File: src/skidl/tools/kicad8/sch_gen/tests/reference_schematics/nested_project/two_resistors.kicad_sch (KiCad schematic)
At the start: 2 parts

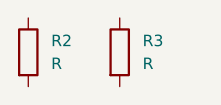
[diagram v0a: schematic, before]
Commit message: add footprint and value to resistors
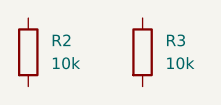
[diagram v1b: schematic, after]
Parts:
- R2, R3: value R -> 10k; footprint (none) -> Resistor_SMD:R_0603_1608Metric
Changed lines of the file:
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@@
-	(symbol
-		(lib_id "Device:R")
-		(at 10.16 0 0)
-		(unit 1)
-		(exclude_from_sim no)
-		(in_bom yes)
-		(on_board yes)
-		(dnp no)
-		(fields_autoplaced yes)
-		(property "Reference" "R3"
-			(at 12.7 -1.2701 0)
-			(effects
-				(font
-					(size 1.27 1.27)
-				)
-				(justify left)
-			)
-		)
-		(property "Value" "R"
-			(at 12.7 1.2699 0)
-			(effects
-				(font
-					(size 1.27 1.27)
-				)
-				(justify left)
-			)
-		)
-		(property "Footprint" ""
-			(at 8.382 0 90)
-			(effects
-				(font
-					(size 1.27 1.27)
-				)
-				(hide yes)
-			)
-		)
-		(property "Datasheet" "~"
-			(at 10.16 0 0)
-			(effects
-				(font
-					(size 1.27 1.27)
-				)
-				(hide yes)
-			)
-		)
-		(property "Description" "Resistor"
-			(at 10.16 0 0)
-			(effects
-				(font
-					(size 1.27 1.27)
-				)
-				(hide yes)
-			)
-		)
-		(pin "2"
-		)
-		(pin "1"
-		)
-		(instances
-			(project "nested_project"
-				(path "/3a480dbf-5a3c-4b90-9d48-bbf5b4cbfeef/9b0b90fc-8973-429f-9882-50bd45935579/69f71eff-1418-4626-afa2-1afed5fbeb27"
-					(reference "R3")
-					(unit 1)
-				)
-			)
-		)
-	)
 	(symbol
 		(lib_id "Device:R")
@@
 			)
 		)
-		(property "Value" "R"
+		(property "Value" "10k"
 			(at 2.54 1.2699 0)
 			(effects
@@
 			)
 		)
-		(property "Footprint" ""
+		(property "Footprint" "Resistor_SMD:R_0603_1608Metric"
 			(at -1.778 0 90)
 			(effects
@@
 					(unit 1)
 				)
+			)
+		)
+	)
+	(symbol
+		(lib_id "Device:R")
+		(at 12.7 0 0)
+		(unit 1)
+		(exclude_from_sim no)
+		(in_bom yes)
+		(on_board yes)
+		(dnp no)
+		(fields_autoplaced yes)
+		(property "Reference" "R3"
+			(at 15.24 -1.2701 0)
+			(effects
+				(font
+					(size 1.27 1.27)
+				)
+				(justify left)
+			)
+		)
+		(property "Value" "10k"
+			(at 15.24 1.2699 0)
+			(effects
+				(font
+					(size 1.27 1.27)
+				)
+				(justify left)
+			)
+		)
+		(property "Footprint" "Resistor_SMD:R_0603_1608Metric"
+			(at 10.922 0 90)
+			(effects
+				(font
+					(size 1.27 1.27)
+				)
+				(hide yes)
+			)
+		)
+		(property "Datasheet" "~"
+			(at 12.7 0 0)
+			(effects
+				(font
+					(size 1.27 1.27)
+				)
+				(hide yes)
+			)
+		)
+		(property "Description" "Resistor"
+			(at 12.7 0 0)
+			(effects
+				(font
+					(size 1.27 1.27)
+				)
+				(hide yes)
+			)
+		)
+		(pin "2"
+		)
+		(pin "1"
+		)
+		(instances
+			(project "nested_project"
+				(path "/3a480dbf-5a3c-4b90-9d48-bbf5b4cbfeef/9b0b90fc-8973-429f-9882-50bd45935579/69f71eff-1418-4626-afa2-1afed5fbeb27"
+					(reference "R3")
+					(unit 1)
+				)
